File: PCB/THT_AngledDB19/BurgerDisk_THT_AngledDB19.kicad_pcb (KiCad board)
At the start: 2 copper layers, 93.7 x 73.4 mm, 18 parts, among them J1 Daisy port in, J2 MicroSD module, J3 UART, J4 Daisy port out, U1 PC817

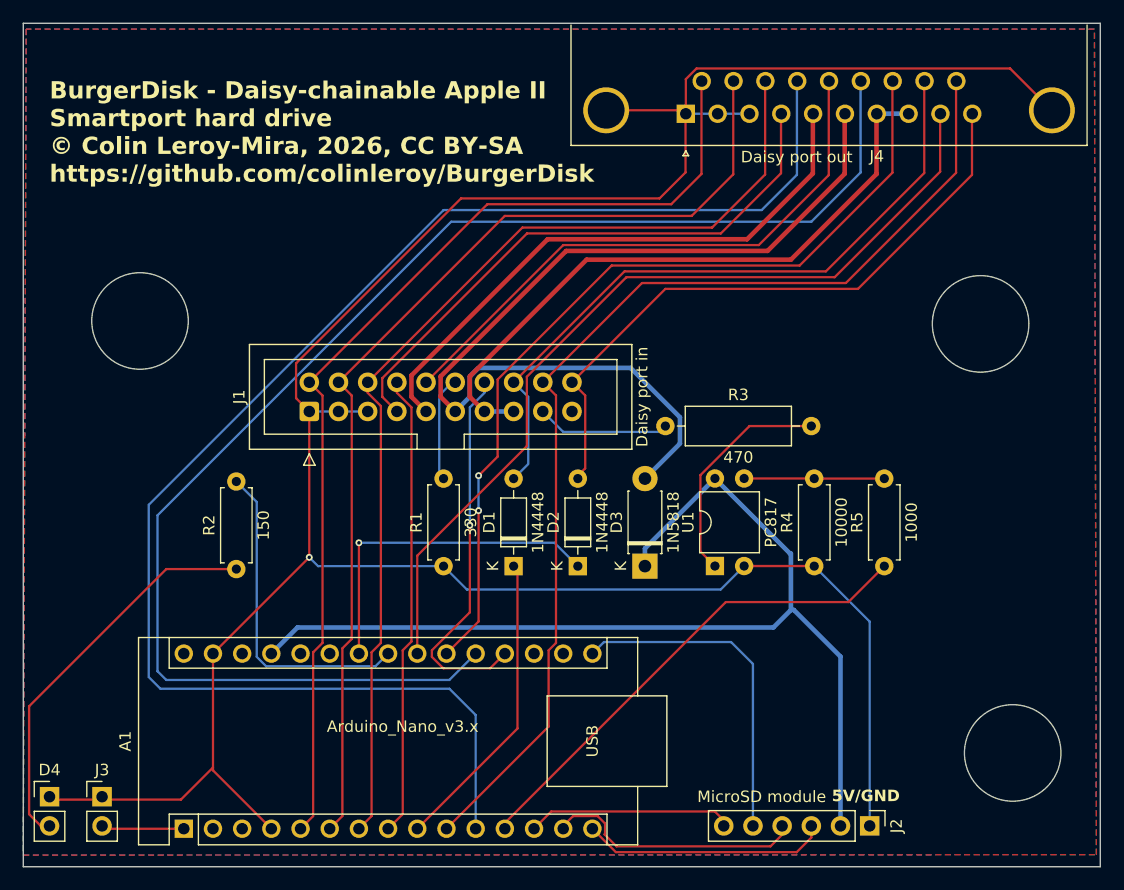
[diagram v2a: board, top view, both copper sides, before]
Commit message: Better routing to allow grounding to ground plane
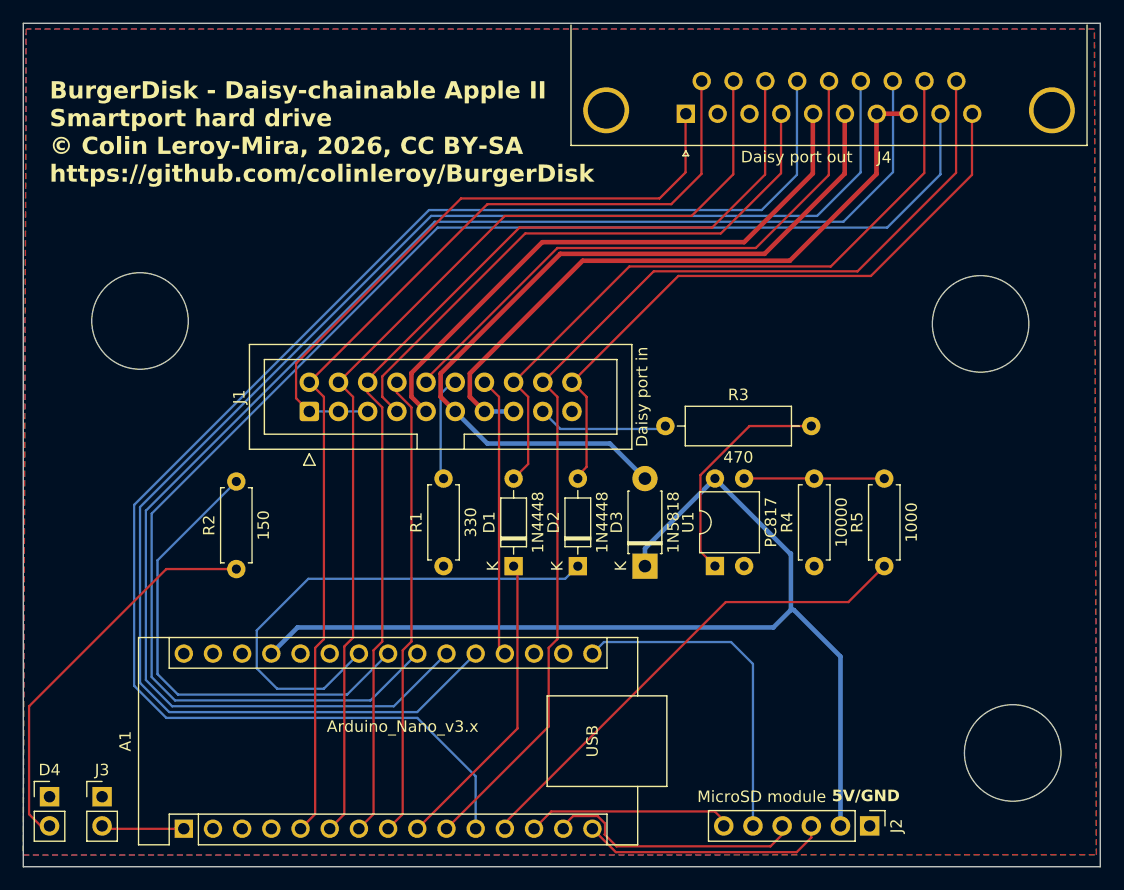
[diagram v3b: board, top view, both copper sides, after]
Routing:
- net GND: track 233.1 -> 56.8 mm, vias 1 -> 0
- net DRV1_out: track 75.5 -> 128.9 mm, vias 2 -> 0
- net DRV2_out: track 76.5 -> 126.0 mm
- net WRPROT_in: track 29.5 -> 44.4 mm, vias 1 -> 0
- net Net-(A1-A4): track 28.2 -> 41.9 mm
- net 5V_apple2: track 81.8 -> 70.4 mm
- net DRV1_in: track 33.1 -> 24.3 mm, vias 1 -> 0
- net HDSEL_out: track 124.0 -> 130.4 mm

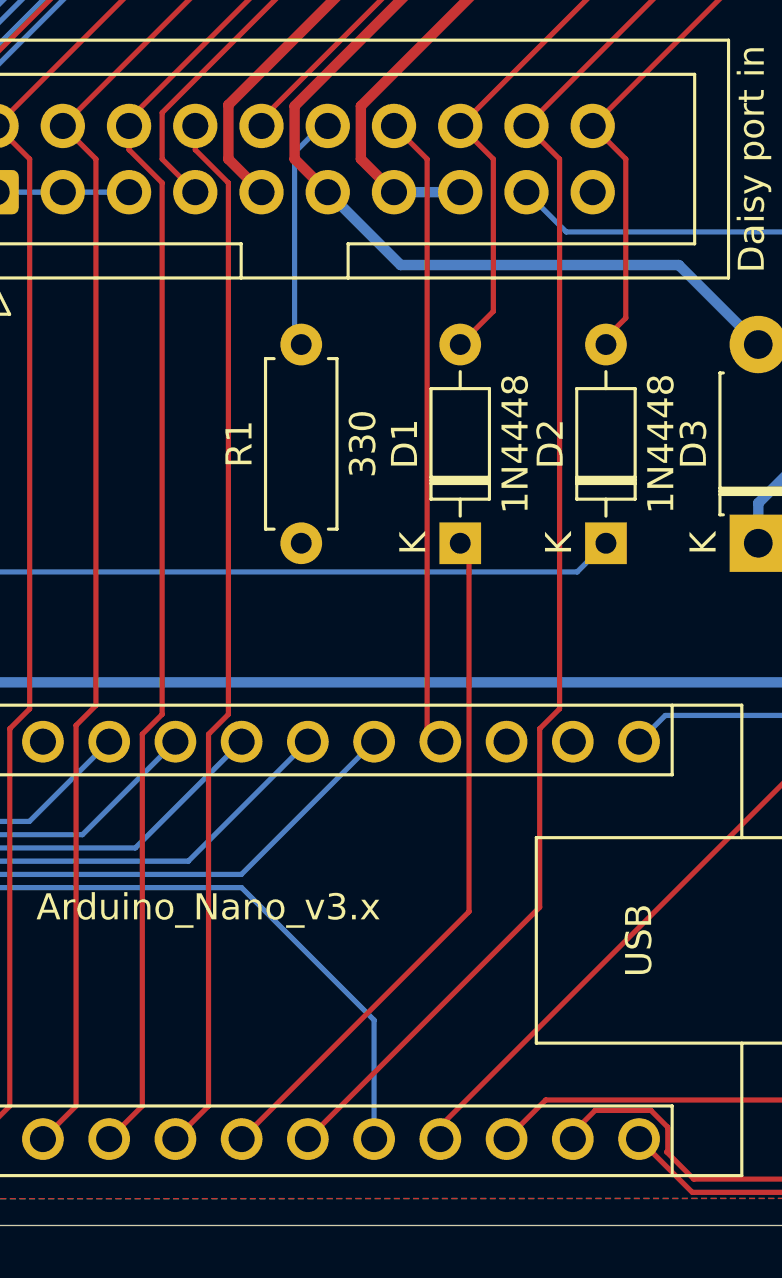
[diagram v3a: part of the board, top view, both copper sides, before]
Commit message: Remove RDDATA diode, causing harm on SoftSP
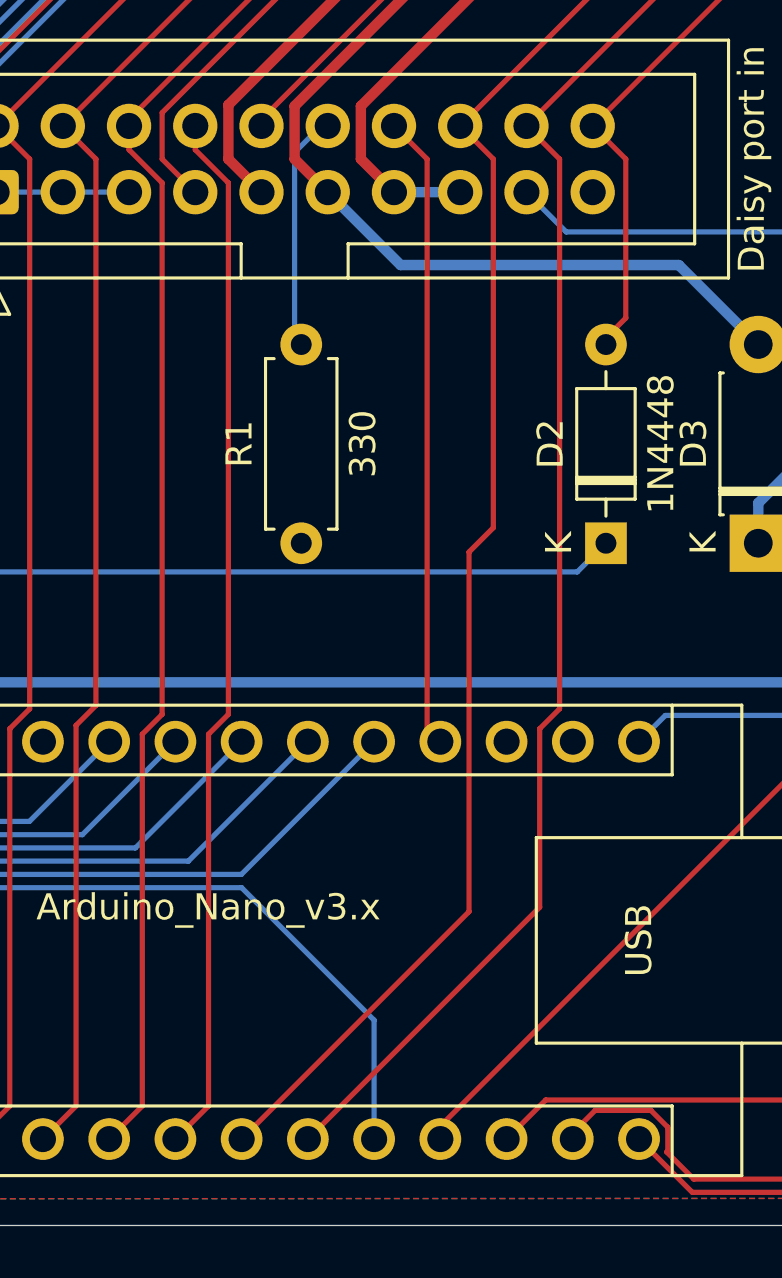
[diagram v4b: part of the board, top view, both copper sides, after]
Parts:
- removed D1: 1N4448, Diode_THT:D_DO-35_SOD27_P7.62mm_Horizontal
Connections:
- J1 pad 16: RDDATA_out -> RDDATA_in
- J4 pad 18: RDDATA_out -> RDDATA_in
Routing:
- net RDDATA_in: track 26.6 -> 94.7 mm
- net RDDATA_out: track 60.7 -> 0.00 mm

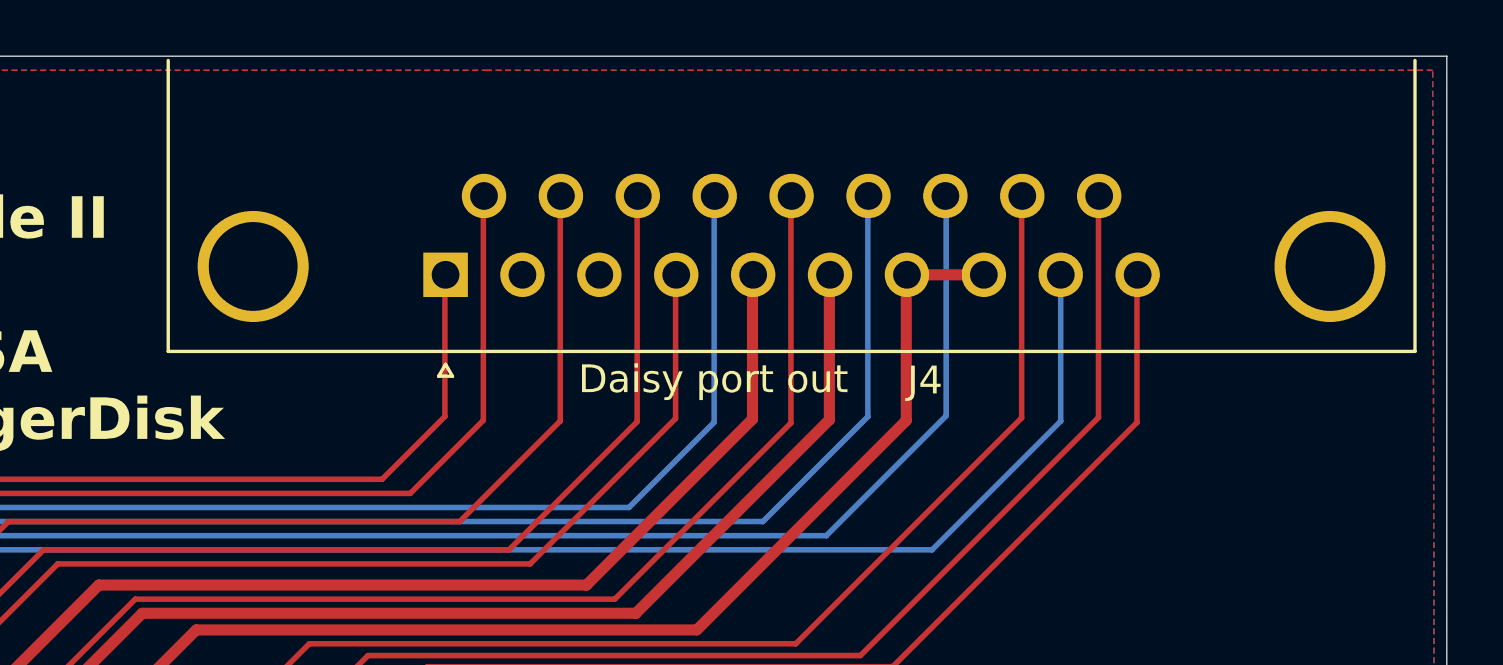
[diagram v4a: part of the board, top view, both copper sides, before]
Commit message: Fix angled DB19 footprint to match the one we can buy
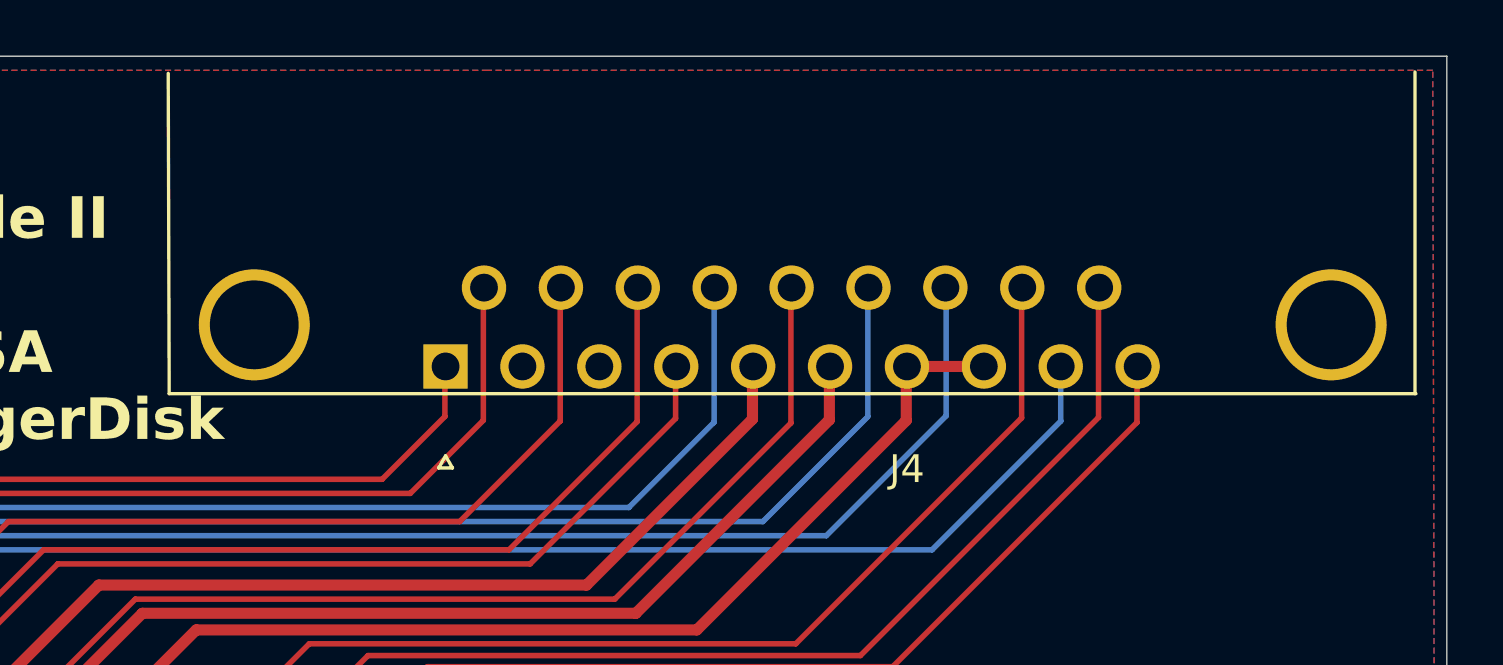
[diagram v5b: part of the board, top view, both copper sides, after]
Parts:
- J4: footprint DSUB-19-angled:DSUB-19_Female_Horizontal_P2.77x2.84mm_EdgePinOffset4.94mm_Housed_MountingHolesOffset7.48mm -> DSUB-19-angled:DSUB-19_Female_Horizontal_MXS82009-8251-9246
- moved J4 3.30 mm to (128.5, 49.0)
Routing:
- net GND: track 56.8 -> 53.1 mm
- net PH1: track 90.2 -> 86.9 mm
- net DRV1_out: track 128.9 -> 125.6 mm
- net WRPROT_out: track 56.9 -> 53.6 mm
- net WRDATA: track 94.9 -> 91.6 mm
- net HDSEL_out: track 130.4 -> 127.1 mm
- net EN3.5: track 50.8 -> 47.5 mm
- net 5V_apple2: track 70.4 -> 67.1 mm
- net WREQ: track 50.9 -> 47.6 mm
- net +12V: track 57.0 -> 53.7 mm
- net RDDATA_in: track 94.7 -> 91.4 mm
- net PH3_out: track 131.0 -> 127.7 mm
- net PH2: track 90.6 -> 87.3 mm
- net PH0: track 89.9 -> 86.6 mm
- net DRV2_out: track 126.0 -> 122.7 mm
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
